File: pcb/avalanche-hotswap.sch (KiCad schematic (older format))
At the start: 104 parts, among them J1 TRRS, J2 LED, J3 OLED, P1 i2c_pin, P2 i2c_pin, SW1 SW_Push, SW10 SW_Push, SW11 SW_Push, SW12 SW_Push, SW13 SW_Push, SW14 SW_Push, SW15 SW_Push, SW16 SW_Push, SW17 SW_Push, SW18 SW_Push, SW19 SW_Push, SW2 SW_Push, SW20 SW_Push, SW21 SW_Push, SW22 SW_Push, SW23 SW_Push, SW24 SW_Push, SW25 SW_Push, SW26 SW_Push, SW27 SW_Push, SW28 SW_Push, SW29 SW_Push, SW3 SW_Push, SW30 SW_Push, SW31 SW_Push, SW32 SW_Push, SW4 SW_Push, SW5 SW_Push, SW6 SW_Push, SW7 SW_Push, SW8 SW_Push, SW9 SW_Push, U1 ProMicro

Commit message: Using different M2 holes.
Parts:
- HM1, HM10, HM11, HM12, HM2, HM3, HM4, HM5, HM6, HM7, HM8, HM9: footprint used_footprints:Hole_Mount_M4 -> used_footprints:M2_HOLE_PCB
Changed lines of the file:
@@
 F 0 "HM1" H 9785 881 50  0000 L CNN
 F 1 "CaseHole" H 9785 790 50  0000 L CNN
-F 2 "used_footprints:Hole_Mount_M4" H 9685 835 50  0001 C CNN
+F 2 "used_footprints:M2_HOLE_PCB" H 9685 835 50  0001 C CNN
 F 3 "~" H 9685 835 50  0001 C CNN
 	1    9685 835
@@
 F 0 "HM2" H 9785 1071 50  0000 L CNN
 F 1 "CaseHole" H 9785 980 50  0000 L CNN
-F 2 "used_footprints:Hole_Mount_M4" H 9685 1025 50  0001 C CNN
+F 2 "used_footprints:M2_HOLE_PCB" H 9685 1025 50  0001 C CNN
 F 3 "~" H 9685 1025 50  0001 C CNN
 	1    9685 1025
@@
 F 0 "HM3" H 9785 1271 50  0000 L CNN
 F 1 "CaseHole" H 9785 1180 50  0000 L CNN
-F 2 "used_footprints:Hole_Mount_M4" H 9685 1225 50  0001 C CNN
+F 2 "used_footprints:M2_HOLE_PCB" H 9685 1225 50  0001 C CNN
 F 3 "~" H 9685 1225 50  0001 C CNN
 	1    9685 1225
@@
 F 0 "HM4" H 9785 1476 50  0000 L CNN
 F 1 "CaseHole" H 9785 1385 50  0000 L CNN
-F 2 "used_footprints:Hole_Mount_M4" H 9685 1430 50  0001 C CNN
+F 2 "used_footprints:M2_HOLE_PCB" H 9685 1430 50  0001 C CNN
 F 3 "~" H 9685 1430 50  0001 C CNN
 	1    9685 1430
@@
 F 0 "HM5" H 9785 1666 50  0000 L CNN
 F 1 "CaseHole" H 9785 1575 50  0000 L CNN
-F 2 "used_footprints:Hole_Mount_M4" H 9685 1620 50  0001 C CNN
+F 2 "used_footprints:M2_HOLE_PCB" H 9685 1620 50  0001 C CNN
 F 3 "~" H 9685 1620 50  0001 C CNN
 	1    9685 1620
@@
 F 0 "HM6" H 9790 1861 50  0000 L CNN
 F 1 "CaseHole" H 9790 1770 50  0000 L CNN
-F 2 "used_footprints:Hole_Mount_M4" H 9690 1815 50  0001 C CNN
+F 2 "used_footprints:M2_HOLE_PCB" H 9690 1815 50  0001 C CNN
 F 3 "~" H 9690 1815 50  0001 C CNN
 	1    9690 1815
@@
 F 0 "HM7" H 10445 896 50  0000 L CNN
 F 1 "CaseHole" H 10445 805 50  0000 L CNN
-F 2 "used_footprints:Hole_Mount_M4" H 10345 850 50  0001 C CNN
+F 2 "used_footprints:M2_HOLE_PCB" H 10345 850 50  0001 C CNN
 F 3 "~" H 10345 850 50  0001 C CNN
 	1    10345 850
@@
 F 0 "HM8" H 10445 1086 50  0000 L CNN
 F 1 "CaseHole" H 10445 995 50  0000 L CNN
-F 2 "used_footprints:Hole_Mount_M4" H 10345 1040 50  0001 C CNN
+F 2 "used_footprints:M2_HOLE_PCB" H 10345 1040 50  0001 C CNN
 F 3 "~" H 10345 1040 50  0001 C CNN
 	1    10345 1040
@@
 F 0 "HM9" H 10445 1286 50  0000 L CNN
 F 1 "CaseHole" H 10445 1195 50  0000 L CNN
-F 2 "used_footprints:Hole_Mount_M4" H 10345 1240 50  0001 C CNN
+F 2 "used_footprints:M2_HOLE_PCB" H 10345 1240 50  0001 C CNN
 F 3 "~" H 10345 1240 50  0001 C CNN
 	1    10345 1240
@@
 F 0 "HM10" H 10445 1491 50  0000 L CNN
 F 1 "CaseHole" H 10445 1400 50  0000 L CNN
-F 2 "used_footprints:Hole_Mount_M4" H 10345 1445 50  0001 C CNN
+F 2 "used_footprints:M2_HOLE_PCB" H 10345 1445 50  0001 C CNN
 F 3 "~" H 10345 1445 50  0001 C CNN
 	1    10345 1445
@@
 F 0 "HM11" H 10445 1681 50  0000 L CNN
 F 1 "CaseHole" H 10445 1590 50  0000 L CNN
-F 2 "used_footprints:Hole_Mount_M4" H 10345 1635 50  0001 C CNN
+F 2 "used_footprints:M2_HOLE_PCB" H 10345 1635 50  0001 C CNN
 F 3 "~" H 10345 1635 50  0001 C CNN
 	1    10345 1635
@@
 F 0 "HM12" H 10450 1876 50  0000 L CNN
 F 1 "CaseHole" H 10450 1785 50  0000 L CNN
-F 2 "used_footprints:Hole_Mount_M4" H 10350 1830 50  0001 C CNN
+F 2 "used_footprints:M2_HOLE_PCB" H 10350 1830 50  0001 C CNN
 F 3 "~" H 10350 1830 50  0001 C CNN
 	1    10350 1830

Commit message: Changed schema
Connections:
- net GND: now also J1.2; no longer J1.4
- net at P1.1 (Pin_1): now also J1.4; no longer J1.2
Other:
- moved on the sheet: P1
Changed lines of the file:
@@
 L power:GND #PWR03
 U 1 1 5E653D30
-P 1545 2875
-F 0 "#PWR03" H 1545 2625 50  0001 C CNN
-F 1 "GND" V 1545 2755 50  0000 R CNN
-F 2 "" H 1545 2875 50  0001 C CNN
-F 3 "" H 1545 2875 50  0001 C CNN
-	1    1545 2875
+P 1545 3125
+F 0 "#PWR03" H 1545 2875 50  0001 C CNN
+F 1 "GND" V 1545 3005 50  0000 R CNN
+F 2 "" H 1545 3125 50  0001 C CNN
+F 3 "" H 1545 3125 50  0001 C CNN
+	1    1545 3125
 	0    -1   -1   0
 $EndComp
@@
 L avalanche-hotswap:i2c_pin P1
 U 1 1 6051604B
-P 2035 2740
-F 0 "P1" V 2035 2805 50  0000 L CNN
-F 1 "i2c_pin" V 2135 2625 50  0000 L CNN
-F 2 "used_footprints:1pin_conn" H 2035 2740 50  0001 C CNN
-F 3 "" H 2035 2740 50  0001 C CNN
-	1    2035 2740
+P 2035 2675
+F 0 "P1" V 2035 2740 50  0000 L CNN
+F 1 "i2c_pin" V 2135 2560 50  0000 L CNN
+F 2 "used_footprints:1pin_conn" H 2035 2675 50  0001 C CNN
+F 3 "" H 2035 2675 50  0001 C CNN
+	1    2035 2675
 	0    -1   -1   0
 $EndComp
@@
 Wire Wire Line
 	1545 3225 2035 3225
-Wire Wire Line
-	2035 2940 2035 3125
-Wire Wire Line
-	2035 3125 1545 3125
 $Comp
 L Mechanical:MountingHole H13
@@
 Wire Wire Line
 	2495 6300 3170 6300
+Wire Wire Line
+	1545 2875 2035 2875
 $EndSCHEMATC

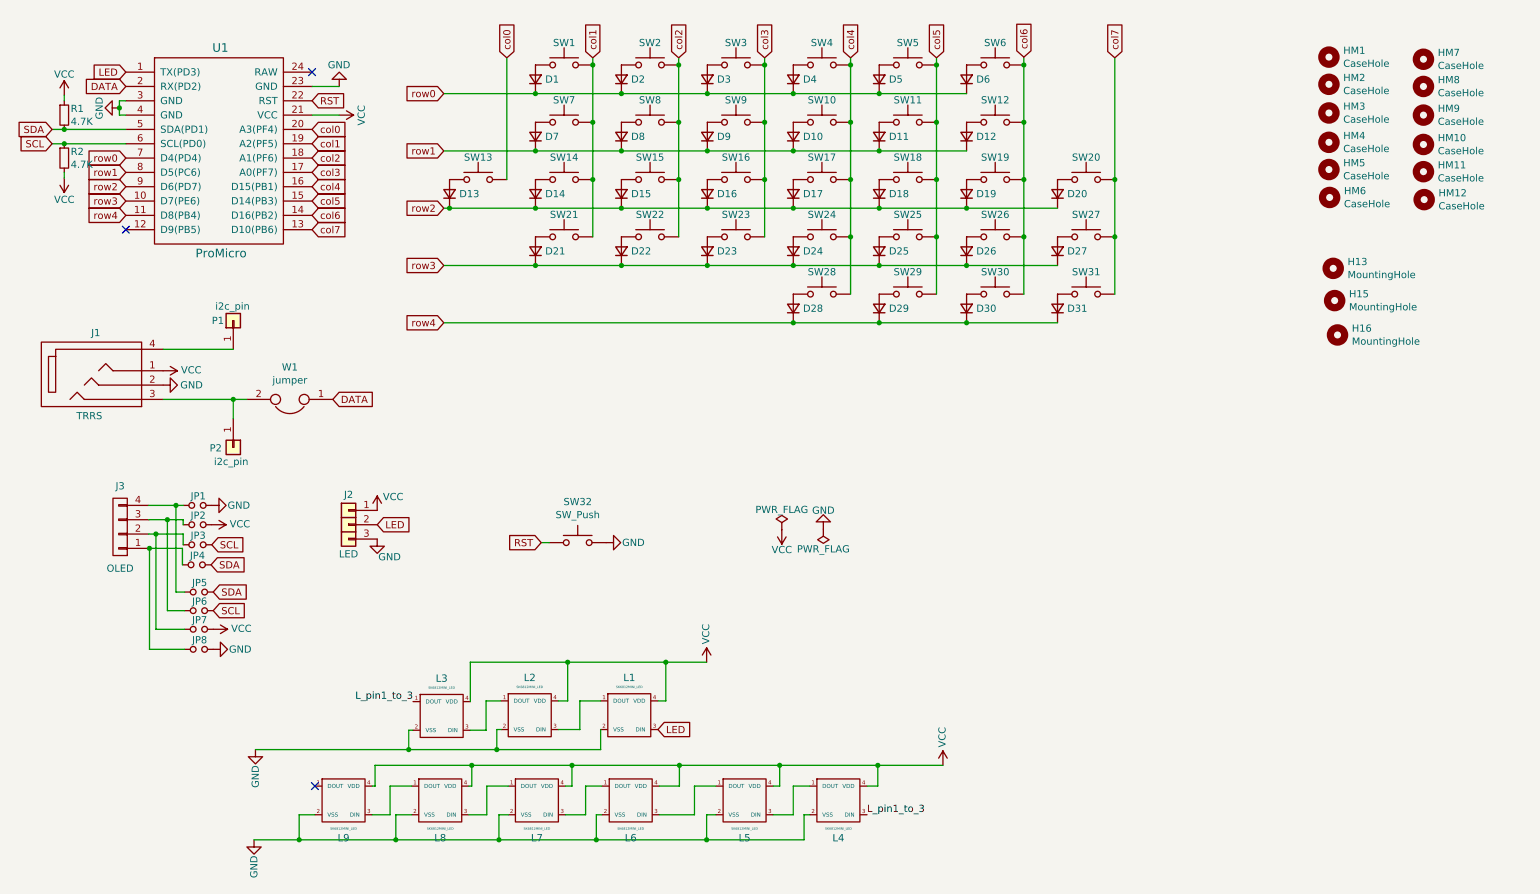
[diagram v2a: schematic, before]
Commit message: - Moved SW13 to a different row and col (needed to free one ProMicro pin) - Added rotary encoders to the scheme - Added rotary encoders footprint
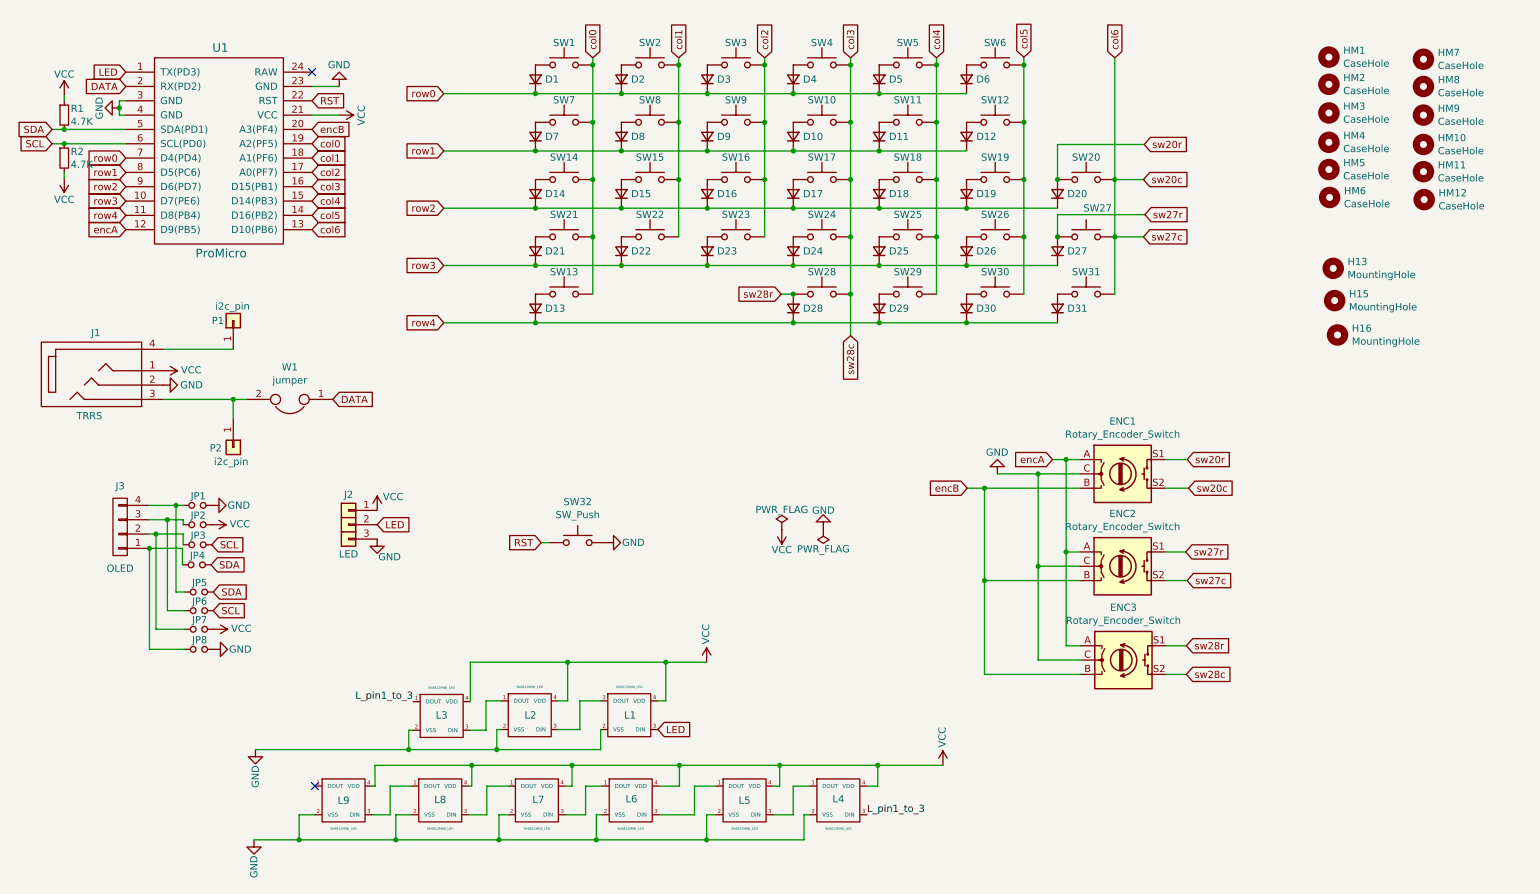
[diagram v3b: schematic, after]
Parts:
- added ENC1, ENC2, ENC3: Rotary_Encoder_Switch, used_footprints:RotaryEncoder_Alps_EC11E-Switch_Vertical_H20mm-keebio_modified, symbol Device:Rotary_Encoder_Switch
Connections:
- net col7 is gone; now on net col6: SW20.2, SW27.2, SW31.2, U1.13 (D10(PB6))
- net GND: now also ENC1.C, ENC2.C, ENC3.C
- net col0: now also SW1.2, SW14.2, SW21.2, SW7.2, U1.19 (A2(PF5)); no longer U1.20 (A3(PF4))
- net col1: now also SW15.2, SW2.2, SW22.2, SW8.2, U1.18 (A1(PF6)); no longer SW1.2, SW14.2, SW21.2, SW7.2, U1.19 (A2(PF5))
- net col2: now also SW16.2, SW23.2, SW3.2, SW9.2, U1.17 (A0(PF7)); no longer SW15.2, SW2.2, SW22.2, SW8.2, U1.18 (A1(PF6))
- net col3: now also SW10.2, SW17.2, SW24.2, SW28.2, SW4.2, U1.16 (D15(PB1)), ENC3.S2; no longer SW16.2, SW23.2, SW3.2, SW9.2, U1.17 (A0(PF7))
- net col4: now also SW11.2, SW18.2, SW25.2, SW29.2, SW5.2, U1.15 (D14(PB3)); no longer SW10.2, SW17.2, SW24.2, SW28.2, SW4.2, U1.16 (D15(PB1))
- net col5: now also SW12.2, SW19.2, SW26.2, SW30.2, SW6.2, U1.14 (D16(PB2)); no longer SW11.2, SW18.2, SW25.2, SW29.2, SW5.2, U1.15 (D14(PB3))
- net col6: now also ENC1.S2, ENC2.S2; no longer SW12.2, SW19.2, SW26.2, SW30.2, SW6.2, U1.14 (D16(PB2))
- net row2: no longer D13.1 (K)
- net row4: now also D13.1 (K)
- net encA: now reaches U1.12 (D9(PB5))
- net encA: now also ENC1.A, ENC2.A, ENC3.A
- net sw28r: now reaches D28.2 (A), SW28.1
- net sw28r: now also ENC3.S1
- net sw20r: now reaches D20.2 (A), SW20.1
- net sw20r: now also ENC1.S1
- net sw27r: now reaches D27.2 (A), SW27.1
- net sw27r: now also ENC2.S1
- new net encB: ENC1.B, ENC2.B, ENC3.B, U1.20 (A3(PF4))
- no-connect marks 3 -> 2
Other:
- moved on the sheet: D13, SW13

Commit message: Routed
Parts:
- R1, R2: footprint used_footprints:RESISTOR_mini -> used_footprints:Resistor_Hybrid_1205
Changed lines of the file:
@@
 U 1 1 5E5A5774
 P 855 1240
-F 0 "R1" H 900 1285 50  0000 L CNN
-F 1 "4.7K" H 900 1195 50  0000 L CNN
-F 2 "used_footprints:RESISTOR_mini" H 855 1240 50  0001 C CNN
+F 0 "R1" H 700 1365 50  0000 L CNN
+F 1 "4.7K" H 640 1285 50  0000 L CNN
+F 2 "used_footprints:Resistor_Hybrid_1205" H 855 1240 50  0001 C CNN
 F 3 "~" H 855 1240 50  0001 C CNN
 	1    855  1240
@@
 U 1 1 5E5A67AE
 P 855 1540
-F 0 "R2" H 900 1585 50  0000 L CNN
-F 1 "4.7K" H 900 1495 50  0000 L CNN
-F 2 "used_footprints:RESISTOR_mini" H 855 1540 50  0001 C CNN
+F 0 "R2" H 705 1540 50  0000 L CNN
+F 1 "4.7K" H 640 1470 50  0000 L CNN
+F 2 "used_footprints:Resistor_Hybrid_1205" H 855 1540 50  0001 C CNN
 F 3 "~" H 855 1540 50  0001 C CNN
 	1    855  1540

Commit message: Changed LEDs to WS2812B
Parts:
- L1, L2, L3, L4, L5, L6, L7, L8, L9: footprint used_footprints:SK6812MINI_underglow_rev -> used_footprints:LED_WS2812B_PLCC4_5.0x5.0mm_P3.2mm
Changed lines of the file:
@@
 F 0 "L3" H 3490 5440 51  0000 C CNN
 F 1 "SK6812MINI_LED" H 3490 5632 16  0000 C CNN
-F 2 "used_footprints:SK6812MINI_underglow_rev" H 3490 5435 60  0001 C CNN
+F 2 "used_footprints:LED_WS2812B_PLCC4_5.0x5.0mm_P3.2mm" H 3490 5435 60  0001 C CNN
 F 3 "" H 3490 5435 60  0001 C CNN
 	1    3490 5435
@@
 F 0 "L2" H 4110 5430 51  0000 C CNN
 F 1 "SK6812MINI_LED" H 4105 5627 16  0000 C CNN
-F 2 "used_footprints:SK6812MINI_underglow_rev" H 4105 5430 60  0001 C CNN
+F 2 "used_footprints:LED_WS2812B_PLCC4_5.0x5.0mm_P3.2mm" H 4105 5430 60  0001 C CNN
 F 3 "" H 4105 5430 60  0001 C CNN
 	1    4105 5430
@@
 F 0 "L1" H 4805 5430 51  0000 C CNN
 F 1 "SK6812MINI_LED" H 4800 5627 16  0000 C CNN
-F 2 "used_footprints:SK6812MINI_underglow_rev" H 4800 5430 60  0001 C CNN
+F 2 "used_footprints:LED_WS2812B_PLCC4_5.0x5.0mm_P3.2mm" H 4800 5430 60  0001 C CNN
 F 3 "" H 4800 5430 60  0001 C CNN
 	1    4800 5430
@@
 F 0 "L8" H 3480 6030 51  0000 C CNN
 F 1 "SK6812MINI_LED" H 3480 5828 16  0000 C CNN
-F 2 "used_footprints:SK6812MINI_underglow_rev" H 3480 6025 60  0001 C CNN
+F 2 "used_footprints:LED_WS2812B_PLCC4_5.0x5.0mm_P3.2mm" H 3480 6025 60  0001 C CNN
 F 3 "" H 3480 6025 60  0001 C CNN
 	1    3480 6025
@@
 F 0 "L7" H 4165 6030 51  0000 C CNN
 F 1 "SK6812MINI_LED" H 4155 5828 16  0000 C CNN
-F 2 "used_footprints:SK6812MINI_underglow_rev" H 4155 6025 60  0001 C CNN
+F 2 "used_footprints:LED_WS2812B_PLCC4_5.0x5.0mm_P3.2mm" H 4155 6025 60  0001 C CNN
 F 3 "" H 4155 6025 60  0001 C CNN
 	1    4155 6025
@@
 F 0 "L6" H 4815 6035 51  0000 C CNN
 F 1 "SK6812MINI_LED" H 4810 5828 16  0000 C CNN
-F 2 "used_footprints:SK6812MINI_underglow_rev" H 4810 6025 60  0001 C CNN
+F 2 "used_footprints:LED_WS2812B_PLCC4_5.0x5.0mm_P3.2mm" H 4810 6025 60  0001 C CNN
 F 3 "" H 4810 6025 60  0001 C CNN
 	1    4810 6025
@@
 F 0 "L5" H 5605 6025 51  0000 C CNN
 F 1 "SK6812MINI_LED" H 5605 5828 16  0000 C CNN
-F 2 "used_footprints:SK6812MINI_underglow_rev" H 5605 6025 60  0001 C CNN
+F 2 "used_footprints:LED_WS2812B_PLCC4_5.0x5.0mm_P3.2mm" H 5605 6025 60  0001 C CNN
 F 3 "" H 5605 6025 60  0001 C CNN
 	1    5605 6025
@@
 F 0 "L4" H 6260 6035 51  0000 C CNN
 F 1 "SK6812MINI_LED" H 6260 5828 16  0000 C CNN
-F 2 "used_footprints:SK6812MINI_underglow_rev" H 6260 6025 60  0001 C CNN
+F 2 "used_footprints:LED_WS2812B_PLCC4_5.0x5.0mm_P3.2mm" H 6260 6025 60  0001 C CNN
 F 3 "" H 6260 6025 60  0001 C CNN
 	1    6260 6025
@@
 F 0 "L9" H 2805 6025 51  0000 C CNN
 F 1 "SK6812MINI_LED" H 2805 5828 16  0000 C CNN
-F 2 "used_footprints:SK6812MINI_underglow_rev" H 2805 6025 60  0001 C CNN
+F 2 "used_footprints:LED_WS2812B_PLCC4_5.0x5.0mm_P3.2mm" H 2805 6025 60  0001 C CNN
 F 3 "" H 2805 6025 60  0001 C CNN
 	1    2805 6025
@@
 Connection ~ 7280 4490
 $Comp
-L power:GND #PWR?
+L power:GND #PWR0111
 U 1 1 6082F9BB
 P 7370 3745
-F 0 "#PWR?" H 7370 3495 50  0001 C CNN
+F 0 "#PWR0111" H 7370 3495 50  0001 C CNN
 F 1 "GND" H 7450 3595 50  0000 R CNN
 F 2 "" H 7370 3745 50  0001 C CNN

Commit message: Started replacing diodes footprints (SMD only).
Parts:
- D1, D2, D3, D4, D5, D6, D7: footprint used_footprints:D3_TH_SMD -> used_footprints:diode_SMD
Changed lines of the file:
@@
 F 0 "D1" V 4145 922 50  0000 R CNN
 F 1 "1N4148" V 4100 922 50  0001 R CNN
-F 2 "used_footprints:D3_TH_SMD" V 4145 990 50  0001 C CNN
+F 2 "used_footprints:diode_SMD" V 4145 990 50  0001 C CNN
 F 3 "~" V 4145 990 50  0001 C CNN
 	1    4145 990
@@
 F 0 "D2" V 4745 922 50  0000 R CNN
 F 1 "1N4148" V 4700 922 50  0001 R CNN
-F 2 "used_footprints:D3_TH_SMD" V 4745 990 50  0001 C CNN
+F 2 "used_footprints:diode_SMD" V 4745 990 50  0001 C CNN
 F 3 "~" V 4745 990 50  0001 C CNN
 	1    4745 990
@@
 F 0 "D3" V 5345 922 50  0000 R CNN
 F 1 "1N4148" V 5300 922 50  0001 R CNN
-F 2 "used_footprints:D3_TH_SMD" V 5345 990 50  0001 C CNN
+F 2 "used_footprints:diode_SMD" V 5345 990 50  0001 C CNN
 F 3 "~" V 5345 990 50  0001 C CNN
 	1    5345 990
@@
 F 0 "D4" V 5945 922 50  0000 R CNN
 F 1 "1N4148" V 5900 922 50  0001 R CNN
-F 2 "used_footprints:D3_TH_SMD" V 5945 990 50  0001 C CNN
+F 2 "used_footprints:diode_SMD" V 5945 990 50  0001 C CNN
 F 3 "~" V 5945 990 50  0001 C CNN
 	1    5945 990
@@
 F 0 "D5" V 6545 922 50  0000 R CNN
 F 1 "1N4148" V 6500 922 50  0001 R CNN
-F 2 "used_footprints:D3_TH_SMD" V 6545 990 50  0001 C CNN
+F 2 "used_footprints:diode_SMD" V 6545 990 50  0001 C CNN
 F 3 "~" V 6545 990 50  0001 C CNN
 	1    6545 990
@@
 F 0 "D7" V 4145 1322 50  0000 R CNN
 F 1 "1N4148" V 4100 1322 50  0001 R CNN
-F 2 "used_footprints:D3_TH_SMD" V 4145 1390 50  0001 C CNN
+F 2 "used_footprints:diode_SMD" V 4145 1390 50  0001 C CNN
 F 3 "~" V 4145 1390 50  0001 C CNN
 	1    4145 1390
@@
 F 0 "D6" V 7155 922 50  0000 R CNN
 F 1 "1N4148" V 7110 922 50  0001 R CNN
-F 2 "used_footprints:D3_TH_SMD" V 7155 990 50  0001 C CNN
+F 2 "used_footprints:diode_SMD" V 7155 990 50  0001 C CNN
 F 3 "~" V 7155 990 50  0001 C CNN
 	1    7155 990

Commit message: WIP on smd diodes...
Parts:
- D10, D11, D12, D8, D9: footprint used_footprints:D3_TH_SMD -> used_footprints:diode_SMD
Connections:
- net L_pin1_to_3: no longer names the net of L3.1 (DOUT), L4.3 (DIN)
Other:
- moved on the sheet: ENC1, ENC2, ENC3, H13, H15, H16, HM1, HM10, HM11, HM12, HM2, HM3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

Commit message: WIP on diodes. Moved a case hole a little bit
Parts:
- D13, D14, D15, D16, D17, D18, D19, D20: footprint used_footprints:D3_TH_SMD -> used_footprints:diode_SMD
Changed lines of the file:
@@
 F 0 "D13" V 4145 2522 50  0000 R CNN
 F 1 "1N4148" V 4100 2522 50  0001 R CNN
-F 2 "used_footprints:D3_TH_SMD" V 4145 2590 50  0001 C CNN
+F 2 "used_footprints:diode_SMD" V 4145 2590 50  0001 C CNN
 F 3 "~" V 4145 2590 50  0001 C CNN
 	1    4145 2590
-	0    -1   -1   0
-$EndComp
-$Comp
-L Device:D_Small D14
-U 1 1 5DAD50E5
-P 4145 1790
-F 0 "D14" V 4145 1722 50  0000 R CNN
-F 1 "1N4148" V 4100 1722 50  0001 R CNN
-F 2 "used_footprints:D3_TH_SMD" V 4145 1790 50  0001 C CNN
-F 3 "~" V 4145 1790 50  0001 C CNN
-	1    4145 1790
 	0    -1   -1   0
 $EndComp
@@
 F 0 "D15" V 4745 1722 50  0000 R CNN
 F 1 "1N4148" V 4700 1722 50  0001 R CNN
-F 2 "used_footprints:D3_TH_SMD" V 4745 1790 50  0001 C CNN
+F 2 "used_footprints:diode_SMD" V 4745 1790 50  0001 C CNN
 F 3 "~" V 4745 1790 50  0001 C CNN
 	1    4745 1790
@@
 F 0 "D16" V 5345 1722 50  0000 R CNN
 F 1 "1N4148" V 5300 1722 50  0001 R CNN
-F 2 "used_footprints:D3_TH_SMD" V 5345 1790 50  0001 C CNN
+F 2 "used_footprints:diode_SMD" V 5345 1790 50  0001 C CNN
 F 3 "~" V 5345 1790 50  0001 C CNN
 	1    5345 1790
@@
 F 0 "D17" V 5945 1722 50  0000 R CNN
 F 1 "1N4148" V 5900 1722 50  0001 R CNN
-F 2 "used_footprints:D3_TH_SMD" V 5945 1790 50  0001 C CNN
+F 2 "used_footprints:diode_SMD" V 5945 1790 50  0001 C CNN
 F 3 "~" V 5945 1790 50  0001 C CNN
 	1    5945 1790
@@
 F 0 "D18" V 6545 1722 50  0000 R CNN
 F 1 "1N4148" V 6500 1722 50  0001 R CNN
-F 2 "used_footprints:D3_TH_SMD" V 6545 1790 50  0001 C CNN
+F 2 "used_footprints:diode_SMD" V 6545 1790 50  0001 C CNN
 F 3 "~" V 6545 1790 50  0001 C CNN
 	1    6545 1790
@@
 Wire Wire Line
 	5945 2290 6545 2290
-Connection ~ 4145 1890
-Wire Wire Line
-	4145 1890 4745 1890
 Connection ~ 4745 1890
 Wire Wire Line
@@
 F 0 "D19" V 7155 1722 50  0000 R CNN
 F 1 "1N4148" V 7110 1722 50  0001 R CNN
-F 2 "used_footprints:D3_TH_SMD" V 7155 1790 50  0001 C CNN
+F 2 "used_footprints:diode_SMD" V 7155 1790 50  0001 C CNN
 F 3 "~" V 7155 1790 50  0001 C CNN
 	1    7155 1790
@@
 F 0 "D20" V 7790 1722 50  0000 R CNN
 F 1 "1N4148" V 7745 1722 50  0001 R CNN
-F 2 "used_footprints:D3_TH_SMD" V 7790 1790 50  0001 C CNN
+F 2 "used_footprints:diode_SMD" V 7790 1790 50  0001 C CNN
 F 3 "~" V 7790 1790 50  0001 C CNN
 	1    7790 1790
@@
 	9150 4490 9820 4490
 Connection ~ 4145 2690
-Wire Wire Line
-	3505 1890 4145 1890
 Wire Wire Line
 	4545 2090 4545 2490
@@
 Connection ~ 7025 5780
 Connection ~ 6535 5780
+Wire Wire Line
+	3505 1890 4145 1890
+Wire Wire Line
+	4145 1890 4745 1890
+Connection ~ 4145 1890
+$Comp
+L Device:D_Small D14
+U 1 1 5DAD50E5
+P 4145 1790
+F 0 "D14" V 4145 1722 50  0000 R CNN
+F 1 "1N4148" V 4100 1722 50  0001 R CNN
+F 2 "used_footprints:diode_SMD" V 4145 1790 50  0001 C CNN
+F 3 "~" V 4145 1790 50  0001 C CNN
+	1    4145 1790
+	0    -1   -1   0
+$EndComp
 $EndSCHEMATC
